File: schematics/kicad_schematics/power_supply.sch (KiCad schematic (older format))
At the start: 28 parts

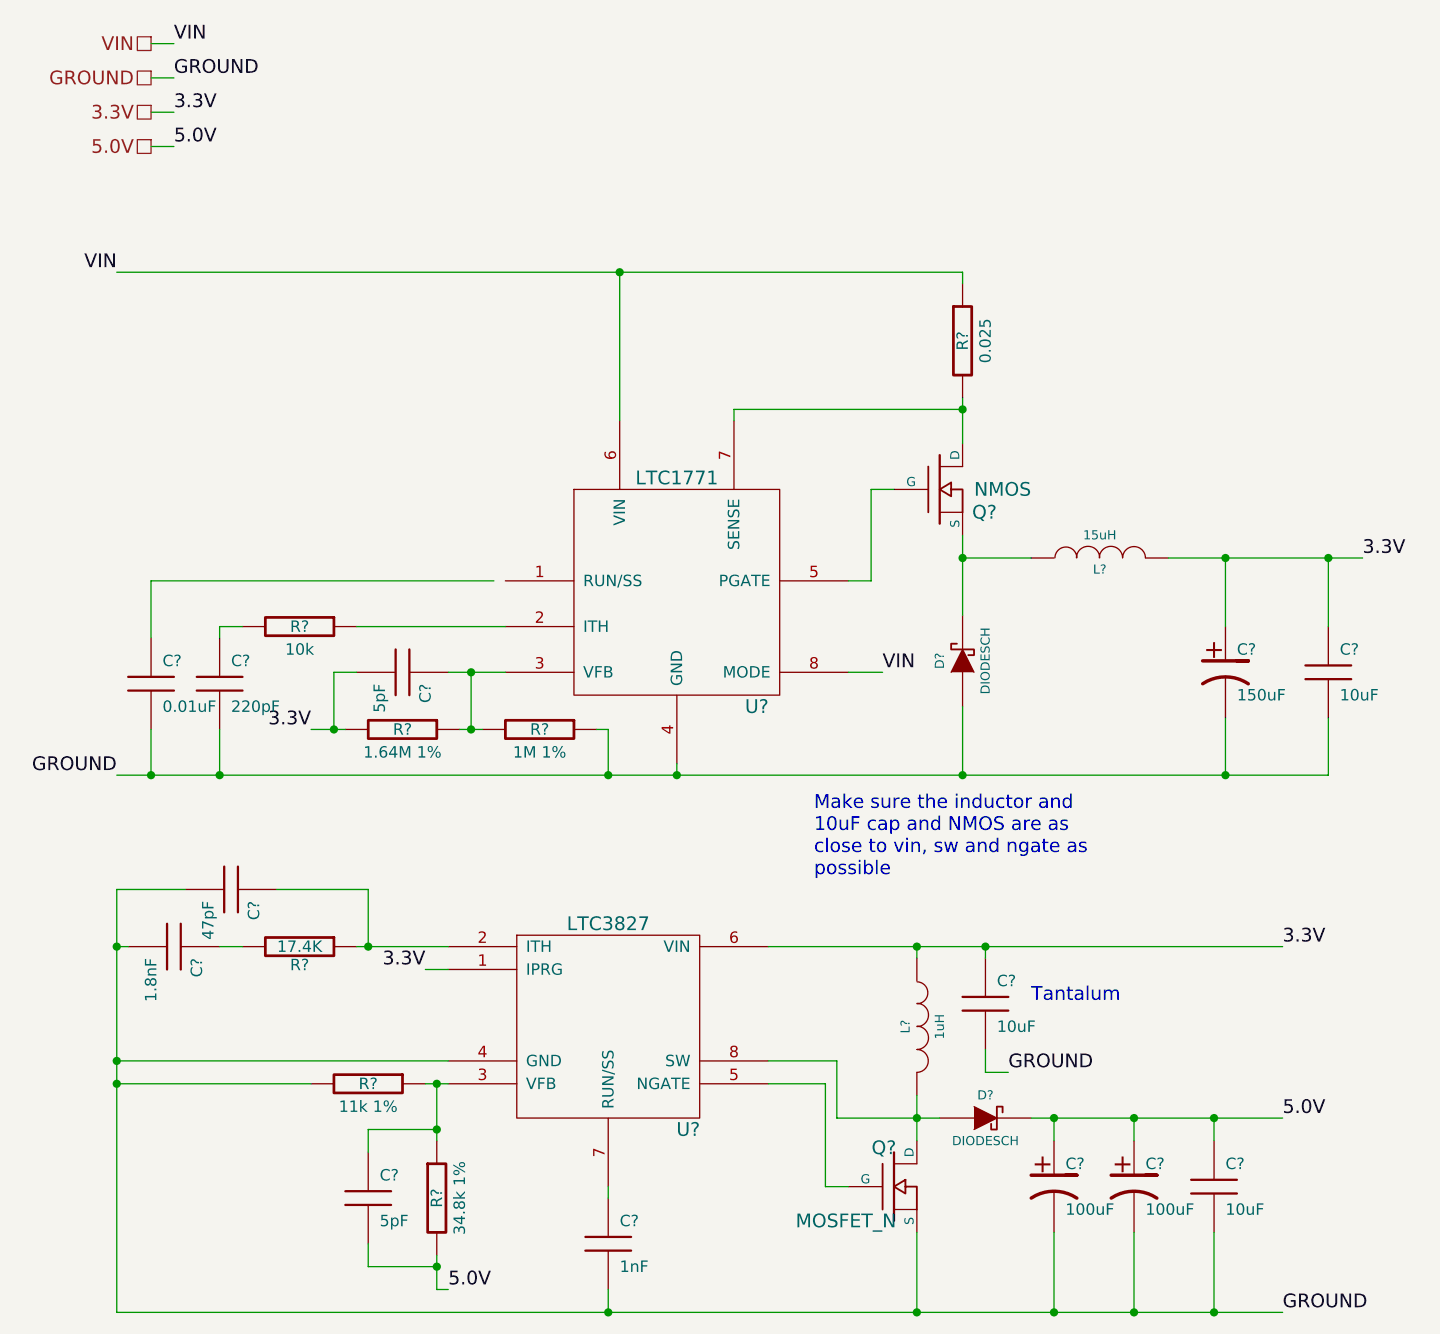
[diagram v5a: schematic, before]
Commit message: Cleaned up Schematic File and modified SD card module, bearboard schematic
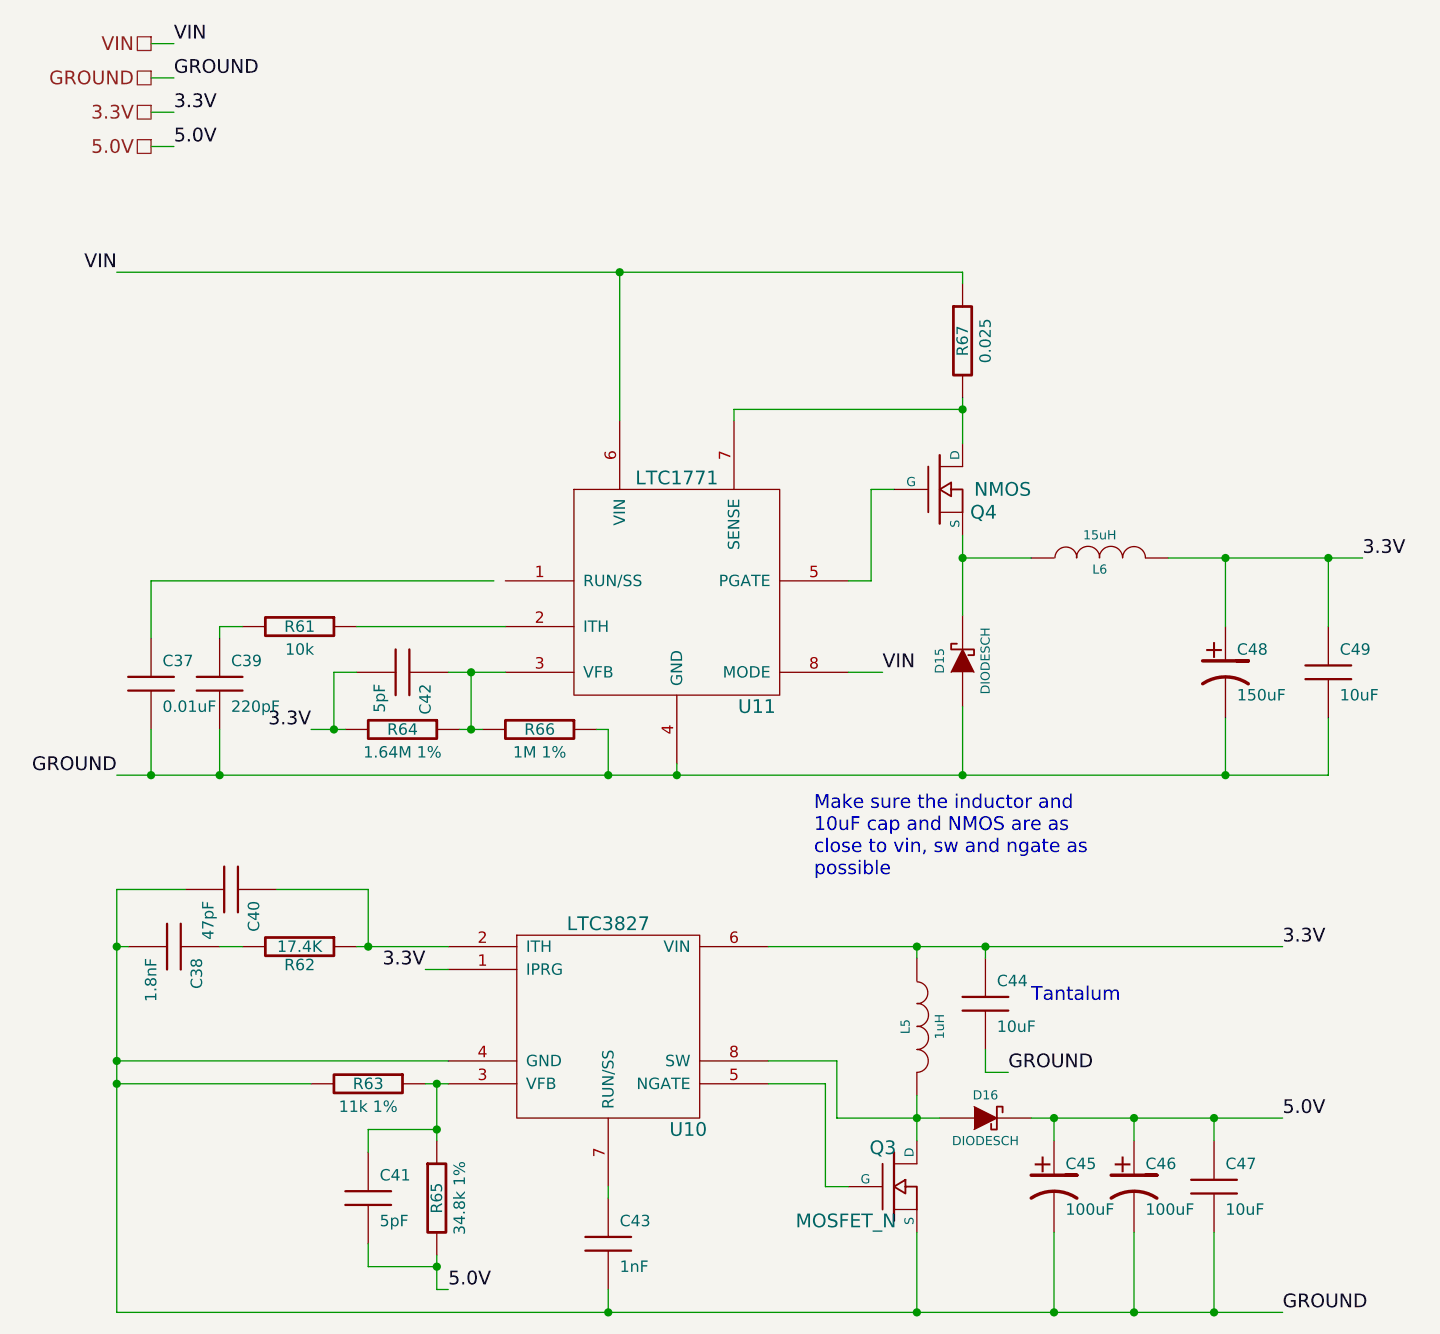
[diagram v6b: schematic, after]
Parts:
- gave numbers to parts that had none: 28
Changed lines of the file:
@@
-EESchema Schematic File Version 2  date Wed 10 Mar 2010 02:43:05 PM EST
+EESchema Schematic File Version 2  date Wed 10 Mar 2010 05:32:05 PM EST
 LIBS:power
 LIBS:device
@@
 5.0V
 $Comp
-L C C?
+L C C40
 U 1 1 4B8A7688
 P 2650 4450
-F 0 "C?" H 2700 4550 50  0000 L CNN
+F 0 "C40" H 2700 4550 50  0000 L CNN
 F 1 "47pF" H 2700 4350 50  0000 L CNN
 	1    2650 4450
@@
 $EndComp
 $Comp
-L C C?
+L C C38
 U 1 1 4B8A767D
 P 2400 4700
-F 0 "C?" H 2450 4800 50  0000 L CNN
+F 0 "C38" H 2450 4800 50  0000 L CNN
 F 1 "1.8nF" H 2450 4600 50  0000 L CNN
 	1    2400 4700
@@
 $EndComp
 $Comp
-L R R?
+L R R62
 U 1 1 4B8A766F
 P 2950 4700
-F 0 "R?" V 3030 4700 50  0000 C CNN
+F 0 "R62" V 3030 4700 50  0000 C CNN
 F 1 "17.4K" V 2950 4700 50  0000 C CNN
 	1    2950 4700
@@
 $EndComp
 $Comp
-L C C?
+L C C41
 U 1 1 4B8A761F
 P 3250 5800
-F 0 "C?" H 3300 5900 50  0000 L CNN
+F 0 "C41" H 3300 5900 50  0000 L CNN
 F 1 "5pF" H 3300 5700 50  0000 L CNN
 	1    3250 5800
@@
 5.0V
 $Comp
-L R R?
+L R R63
 U 1 1 4B8A758D
 P 3250 5300
-F 0 "R?" V 3250 5300 50  0000 C CNN
+F 0 "R63" V 3250 5300 50  0000 C CNN
 F 1 "11k 1%" V 3350 5300 50  0000 C CNN
 	1    3250 5300
@@
 $EndComp
 $Comp
-L R R?
+L R R65
 U 1 1 4B8A7583
 P 3550 5800
-F 0 "R?" V 3550 5800 50  0000 C CNN
+F 0 "R65" V 3550 5800 50  0000 C CNN
 F 1 "34.8k 1%" V 3650 5800 50  0000 C CNN
 	1    3550 5800
@@
 $EndComp
 $Comp
-L C C?
+L C C43
 U 1 1 4B8A753A
 P 4300 6000
-F 0 "C?" H 4350 6100 50  0000 L CNN
+F 0 "C43" H 4350 6100 50  0000 L CNN
 F 1 "1nF" H 4350 5900 50  0000 L CNN
 	1    4300 6000
@@
 GROUND
 $Comp
-L C C?
+L C C44
 U 1 1 4B8A7462
 P 5950 4950
-F 0 "C?" H 6000 5050 50  0000 L CNN
+F 0 "C44" H 6000 5050 50  0000 L CNN
 F 1 "10uF" H 6000 4850 50  0000 L CNN
 	1    5950 4950
@@
 GROUND
 $Comp
-L C C?
+L C C47
 U 1 1 4B8A73D4
 P 6950 5750
-F 0 "C?" H 7000 5850 50  0000 L CNN
+F 0 "C47" H 7000 5850 50  0000 L CNN
 F 1 "10uF" H 7000 5650 50  0000 L CNN
 	1    6950 5750
@@
 $EndComp
 $Comp
-L CP1 C?
+L CP1 C46
 U 1 1 4B8A73CB
 P 6600 5750
-F 0 "C?" H 6650 5850 50  0000 L CNN
+F 0 "C46" H 6650 5850 50  0000 L CNN
 F 1 "100uF" H 6650 5650 50  0000 L CNN
 	1    6600 5750
@@
 $EndComp
 $Comp
-L CP1 C?
+L CP1 C45
 U 1 1 4B8A73BE
 P 6250 5750
-F 0 "C?" H 6300 5850 50  0000 L CNN
+F 0 "C45" H 6300 5850 50  0000 L CNN
 F 1 "100uF" H 6300 5650 50  0000 L CNN
 	1    6250 5750
@@
 $EndComp
 $Comp
-L DIODESCH D?
+L DIODESCH D16
 U 1 1 4B8A73A8
 P 5950 5450
-F 0 "D?" H 5950 5550 40  0000 C CNN
+F 0 "D16" H 5950 5550 40  0000 C CNN
 F 1 "DIODESCH" H 5950 5350 40  0000 C CNN
 	1    5950 5450
@@
 $EndComp
 $Comp
-L INDUCTOR L?
+L INDUCTOR L5
 U 1 1 4B8A7363
 P 5650 5050
-F 0 "L?" V 5600 5050 40  0000 C CNN
+F 0 "L5" V 5600 5050 40  0000 C CNN
 F 1 "1uH" V 5750 5050 40  0000 C CNN
 	1    5650 5050
@@
 $EndComp
 $Comp
-L MOSFET_N Q?
+L MOSFET_N Q3
 U 1 1 4B8A7345
 P 5550 5750
-F 0 "Q?" H 5560 5920 60  0000 R CNN
+F 0 "Q3" H 5560 5920 60  0000 R CNN
 F 1 "MOSFET_N" H 5560 5600 60  0000 R CNN
 	1    5550 5750
@@
 $EndComp
 $Comp
-L LTC3827 U?
+L LTC3827 U10
 U 1 1 4B8A7318
 P 4300 5050
-F 0 "U?" H 4650 4600 60  0000 C CNN
+F 0 "U10" H 4650 4600 60  0000 C CNN
 F 1 "LTC3827" H 4300 5500 60  0000 C CNN
 	1    4300 5050
@@
 3.3V
 $Comp
-L C C?
+L C C42
 U 1 1 4B893539
 P 3400 3500
-F 0 "C?" H 3450 3600 50  0000 L CNN
+F 0 "C42" H 3450 3600 50  0000 L CNN
 F 1 "5pF" H 3450 3400 50  0000 L CNN
 	1    3400 3500
@@
 $EndComp
 $Comp
-L R R?
+L R R66
 U 1 1 4B893528
 P 4000 3750
-F 0 "R?" V 4000 3750 50  0000 C CNN
+F 0 "R66" V 4000 3750 50  0000 C CNN
 F 1 "1M 1%" V 4100 3750 50  0000 C CNN
 	1    4000 3750
@@
 $EndComp
 $Comp
-L R R?
+L R R64
 U 1 1 4B893518
 P 3400 3750
-F 0 "R?" V 3400 3750 50  0000 C CNN
+F 0 "R64" V 3400 3750 50  0000 C CNN
 F 1 "1.64M 1%" V 3500 3750 50  0000 C CNN
 	1    3400 3750
@@
 $EndComp
 $Comp
-L C C?
+L C C39
 U 1 1 4B8934DD
 P 2600 3550
-F 0 "C?" H 2650 3650 50  0000 L CNN
+F 0 "C39" H 2650 3650 50  0000 L CNN
 F 1 "220pF" H 2650 3450 50  0000 L CNN
 	1    2600 3550
@@
 $EndComp
 $Comp
-L R R?
+L R R61
 U 1 1 4B8934CE
 P 2950 3300
-F 0 "R?" V 2950 3300 50  0000 C CNN
+F 0 "R61" V 2950 3300 50  0000 C CNN
 F 1 "10k" V 3050 3300 50  0000 C CNN
 	1    2950 3300
@@
 $EndComp
 $Comp
-L C C?
+L C C37
 U 1 1 4B8934B4
 P 2300 3550
-F 0 "C?" H 2350 3650 50  0000 L CNN
+F 0 "C37" H 2350 3650 50  0000 L CNN
 F 1 "0.01uF" H 2350 3450 50  0000 L CNN
 	1    2300 3550
@@
 $EndComp
 $Comp
-L C C?
+L C C49
 U 1 1 4B893480
 P 7450 3500
-F 0 "C?" H 7500 3600 50  0000 L CNN
+F 0 "C49" H 7500 3600 50  0000 L CNN
 F 1 "10uF" H 7500 3400 50  0000 L CNN
 	1    7450 3500
@@
 VIN
 $Comp
-L CP1 C?
+L CP1 C48
 U 1 1 4B89335E
 P 7000 3500
-F 0 "C?" H 7050 3600 50  0000 L CNN
+F 0 "C48" H 7050 3600 50  0000 L CNN
 F 1 "150uF" H 7050 3400 50  0000 L CNN
 	1    7000 3500
@@
 $EndComp
 $Comp
-L INDUCTOR L?
+L INDUCTOR L6
 U 1 1 4B8932D4
 P 6450 3000
-F 0 "L?" V 6400 3000 40  0000 C CNN
+F 0 "L6" V 6400 3000 40  0000 C CNN
 F 1 "15uH" V 6550 3000 40  0000 C CNN
 	1    6450 3000
@@
 VIN
 $Comp
-L DIODESCH D?
+L DIODESCH D15
 U 1 1 4B8931FF
 P 5850 3450
-F 0 "D?" H 5850 3550 40  0000 C CNN
+F 0 "D15" H 5850 3550 40  0000 C CNN
 F 1 "DIODESCH" H 5850 3350 40  0000 C CNN
 	1    5850 3450
@@
 $EndComp
 $Comp
-L R R?
+L R R67
 U 1 1 4B893191
 P 5850 2050
-F 0 "R?" V 5850 2050 50  0000 C CNN
+F 0 "R67" V 5850 2050 50  0000 C CNN
 F 1 "0.025" V 5950 2050 50  0000 C CNN
 	1    5850 2050
@@
 $EndComp
 $Comp
-L MOSFET_N Q?
+L MOSFET_N Q4
 U 1 1 4B893175
 P 5750 2700
-F 0 "Q?" H 6000 2600 60  0000 R CNN
+F 0 "Q4" H 6000 2600 60  0000 R CNN
 F 1 "NMOS" H 6150 2700 60  0000 R CNN
 	1    5750 2700
@@
 $EndComp
 $Comp
-L LTC1771 U?
+L LTC1771 U11
 U 1 1 4B893166
 P 4600 3150
-F 0 "U?" H 4950 2650 60  0000 C CNN
+F 0 "U11" H 4950 2650 60  0000 C CNN
 F 1 "LTC1771" H 4600 3650 60  0000 C CNN
 	1    4600 3150

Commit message: Updated USB connector to change the sheild pin to power input Updated the schematic to fix some schematic electrical issues
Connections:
- net at U11.1 (RUN/SS): now also C37.1
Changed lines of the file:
@@
-EESchema Schematic File Version 2  date Wed 10 Mar 2010 05:32:05 PM EST
+EESchema Schematic File Version 2  date Wed 10 Mar 2010 08:20:30 PM EST
 LIBS:power
 LIBS:device
@@
 EELAYER END
 $Descr A4 11700 8267
-Sheet 2 5
+Sheet 3 5
 Title ""
-Date "10 mar 2010"
+Date "11 mar 2010"
 Rev ""
 Comp ""
@@
 Comment4 ""
 $EndDescr
+Wire Wire Line
+	3850 3100 2300 3100
+Connection ~ 2150 4700
+Connection ~ 2150 5200
+Wire Wire Line
+	2150 4450 2150 6300
+Wire Wire Line
+	2150 4450 2450 4450
+Wire Wire Line
+	2150 4700 2200 4700
+Wire Wire Line
+	3200 4700 3600 4700
+Connection ~ 3550 5500
+Wire Wire Line
+	3550 5500 3250 5500
+Wire Wire Line
+	3250 5500 3250 5600
+Wire Wire Line
+	3000 5300 2150 5300
+Wire Wire Line
+	2150 5200 3600 5200
+Wire Wire Line
+	3600 5300 3500 5300
+Wire Wire Line
+	3600 6200 3550 6200
+Wire Wire Line
+	3550 6200 3550 6050
+Connection ~ 5650 6300
+Wire Wire Line
+	4300 6200 4300 6300
+Connection ~ 5950 4700
+Wire Wire Line
+	5950 4700 5950 4750
+Connection ~ 5650 4700
+Wire Wire Line
+	5000 4700 7250 4700
+Wire Wire Line
+	6950 6300 6950 5950
+Connection ~ 6250 6300
+Wire Wire Line
+	6250 6300 6250 5950
+Connection ~ 6250 5450
+Wire Wire Line
+	6250 5450 6250 5550
+Wire Wire Line
+	6950 5550 6950 5450
+Wire Wire Line
+	5350 5750 5250 5750
+Wire Wire Line
+	5250 5750 5250 5300
+Wire Wire Line
+	5250 5300 5000 5300
+Wire Wire Line
+	5650 5550 5650 5350
+Wire Wire Line
+	2300 1050 2400 1050
+Wire Wire Line
+	2300 750  2400 750
+Wire Wire Line
+	3100 3750 3100 3500
+Wire Wire Line
+	3100 3500 3200 3500
+Connection ~ 3700 3750
+Wire Wire Line
+	3700 3750 3700 3500
+Connection ~ 4300 3950
+Wire Wire Line
+	4300 3950 4300 3750
+Wire Wire Line
+	4300 3750 4250 3750
+Wire Wire Line
+	3200 3300 3850 3300
+Connection ~ 2300 3950
+Wire Wire Line
+	2300 3750 2300 3950
+Connection ~ 7000 3950
+Wire Wire Line
+	2150 3950 7450 3950
+Wire Wire Line
+	7450 3950 7450 3700
+Wire Wire Line
+	7600 3000 6750 3000
+Wire Wire Line
+	5500 3500 5350 3500
+Wire Wire Line
+	7000 3000 7000 3300
+Connection ~ 4600 3950
+Wire Wire Line
+	2150 1750 5850 1750
+Wire Wire Line
+	5350 3100 5450 3100
+Wire Wire Line
+	5450 3100 5450 2700
+Wire Wire Line
+	5450 2700 5550 2700
+Wire Wire Line
+	4350 2400 4350 1750
+Wire Wire Line
+	5850 1750 5850 1800
+Wire Wire Line
+	5850 2500 5850 2300
+Wire Wire Line
+	5850 2350 4850 2350
+Wire Wire Line
+	4850 2350 4850 2400
+Connection ~ 5850 2350
+Wire Wire Line
+	5850 3250 5850 2900
+Connection ~ 4350 1750
+Wire Wire Line
+	5850 3950 5850 3650
+Wire Wire Line
+	4600 3950 4600 3900
+Wire Wire Line
+	6150 3000 5850 3000
+Connection ~ 5850 3000
+Wire Wire Line
+	7000 3700 7000 3950
+Connection ~ 5850 3950
+Connection ~ 7000 3000
+Wire Wire Line
+	7450 3300 7450 3000
+Connection ~ 7450 3000
+Wire Wire Line
+	2600 3350 2600 3300
+Wire Wire Line
+	2600 3300 2700 3300
+Wire Wire Line
+	2600 3950 2600 3750
+Connection ~ 2600 3950
+Wire Wire Line
+	3750 3750 3650 3750
+Wire Wire Line
+	3850 3500 3600 3500
+Connection ~ 3700 3500
+Wire Wire Line
+	3000 3750 3150 3750
+Connection ~ 3100 3750
+Wire Wire Line
+	2300 900  2400 900
+Wire Wire Line
+	5650 4750 5650 4700
+Wire Wire Line
+	5000 5200 5300 5200
+Wire Wire Line
+	5300 5200 5300 5450
+Connection ~ 5650 5450
+Wire Wire Line
+	5300 5450 5750 5450
+Wire Wire Line
+	6600 5450 6600 5550
+Connection ~ 6600 5450
+Wire Wire Line
+	5650 6300 5650 5950
+Wire Wire Line
+	6600 6300 6600 5950
+Connection ~ 6600 6300
+Connection ~ 6950 6300
+Wire Wire Line
+	5950 5150 5950 5250
+Wire Wire Line
+	5950 5250 6050 5250
+Wire Wire Line
+	7250 5450 6150 5450
+Connection ~ 6950 5450
+Wire Wire Line
+	4300 5800 4300 5750
+Wire Wire Line
+	3600 4800 3500 4800
+Wire Wire Line
+	3550 5550 3550 5300
+Connection ~ 3550 5300
+Wire Wire Line
+	2150 6300 7250 6300
+Connection ~ 4300 6300
+Connection ~ 2150 5300
+Wire Wire Line
+	3250 6000 3250 6100
+Wire Wire Line
+	3250 6100 3550 6100
+Connection ~ 3550 6100
+Wire Wire Line
+	2700 4700 2600 4700
+Wire Wire Line
+	2850 4450 3250 4450
+Wire Wire Line
+	3250 4450 3250 4700
+Connection ~ 3250 4700
+Wire Wire Line
+	2300 1200 2400 1200
+Wire Wire Line
+	2300 3100 2300 3350
 Text Label 2400 1200 0    60   ~ 0
 5.0V
-Wire Wire Line
-	2300 1200 2400 1200
-Connection ~ 3250 4700
-Wire Wire Line
-	3250 4700 3250 4450
-Wire Wire Line
-	3250 4450 2850 4450
-Wire Wire Line
-	2700 4700 2600 4700
-Connection ~ 3550 6100
-Wire Wire Line
-	3550 6100 3250 6100
-Wire Wire Line
-	3250 6100 3250 6000
-Connection ~ 2150 5300
-Connection ~ 4300 6300
-Wire Wire Line
-	7250 6300 2150 6300
-Connection ~ 3550 5300
-Wire Wire Line
-	3550 5550 3550 5300
-Wire Wire Line
-	3600 4800 3500 4800
-Wire Wire Line
-	4300 5800 4300 5750
-Connection ~ 6950 5450
-Wire Wire Line
-	7250 5450 6150 5450
-Wire Wire Line
-	6050 5250 5950 5250
-Wire Wire Line
-	5950 5250 5950 5150
-Connection ~ 6950 6300
-Connection ~ 6600 6300
-Wire Wire Line
-	6600 6300 6600 5950
-Wire Wire Line
-	5650 6300 5650 5950
-Connection ~ 6600 5450
-Wire Wire Line
-	6600 5450 6600 5550
-Wire Wire Line
-	5750 5450 5300 5450
-Connection ~ 5650 5450
-Wire Wire Line
-	5300 5450 5300 5200
-Wire Wire Line
-	5300 5200 5000 5200
-Wire Wire Line
-	5650 4750 5650 4700
-Wire Wire Line
-	2300 900  2400 900
-Connection ~ 3100 3750
-Wire Wire Line
-	3000 3750 3150 3750
-Connection ~ 3700 3500
-Wire Wire Line
-	3850 3500 3600 3500
-Wire Wire Line
-	3750 3750 3650 3750
-Connection ~ 2600 3950
-Wire Wire Line
-	2600 3950 2600 3750
-Wire Wire Line
-	2700 3300 2600 3300
-Wire Wire Line
-	2600 3300 2600 3350
-Wire Wire Line
-	2300 3350 2300 3100
-Wire Wire Line
-	2300 3100 3800 3100
-Connection ~ 7450 3000
-Wire Wire Line
-	7450 3300 7450 3000
-Connection ~ 7000 3000
-Connection ~ 5850 3950
-Wire Wire Line
-	7000 3700 7000 3950
-Connection ~ 5850 3000
-Wire Wire Line
-	6150 3000 5850 3000
-Wire Wire Line
-	4600 3950 4600 3900
-Wire Wire Line
-	5850 3950 5850 3650
-Connection ~ 4350 1750
-Wire Wire Line
-	5850 3250 5850 2900
-Connection ~ 5850 2350
-Wire Wire Line
-	4850 2400 4850 2350
-Wire Wire Line
-	4850 2350 5850 2350
-Wire Wire Line
-	5850 2500 5850 2300
-Wire Wire Line
-	5850 1800 5850 1750
-Wire Wire Line
-	4350 2400 4350 1750
-Wire Wire Line
-	5550 2700 5450 2700
-Wire Wire Line
-	5450 2700 5450 3100
-Wire Wire Line
-	5450 3100 5350 3100
-Wire Wire Line
-	5850 1750 2150 1750
-Connection ~ 4600 3950
-Wire Wire Line
-	7000 3000 7000 3300
-Wire Wire Line
-	5500 3500 5350 3500
-Wire Wire Line
-	7600 3000 6750 3000
-Wire Wire Line
-	7450 3700 7450 3950
-Wire Wire Line
-	7450 3950 2150 3950
-Connection ~ 7000 3950
-Wire Wire Line
-	2300 3750 2300 3950
-Connection ~ 2300 3950
-Wire Wire Line
-	3200 3300 3850 3300
-Wire Wire Line
-	4250 3750 4300 3750
-Wire Wire Line
-	4300 3750 4300 3950
-Connection ~ 4300 3950
-Wire Wire Line
-	3700 3750 3700 3500
-Connection ~ 3700 3750
-Wire Wire Line
-	3200 3500 3100 3500
-Wire Wire Line
-	3100 3500 3100 3750
-Wire Wire Line
-	2300 750  2400 750
-Wire Wire Line
-	2300 1050 2400 1050
-Wire Wire Line
-	5650 5550 5650 5350
-Wire Wire Line
-	5000 5300 5250 5300
-Wire Wire Line
-	5250 5300 5250 5750
-Wire Wire Line
-	5250 5750 5350 5750
-Wire Wire Line
-	6950 5550 6950 5450
-Wire Wire Line
-	6250 5450 6250 5550
-Connection ~ 6250 5450
-Wire Wire Line
-	6250 6300 6250 5950
-Connection ~ 6250 6300
-Wire Wire Line
-	6950 6300 6950 5950
-Wire Wire Line
-	5000 4700 7250 4700
-Connection ~ 5650 4700
-Wire Wire Line
-	5950 4700 5950 4750
-Connection ~ 5950 4700
-Wire Wire Line
-	4300 6200 4300 6300
-Connection ~ 5650 6300
-Wire Wire Line
-	3550 6050 3550 6200
-Wire Wire Line
-	3550 6200 3600 6200
-Wire Wire Line
-	3600 5300 3500 5300
-Wire Wire Line
-	2150 5200 3600 5200
-Wire Wire Line
-	3000 5300 2150 5300
-Wire Wire Line
-	3250 5600 3250 5500
-Wire Wire Line
-	3250 5500 3550 5500
-Connection ~ 3550 5500
-Wire Wire Line
-	3200 4700 3600 4700
-Wire Wire Line
-	2150 4700 2200 4700
-Wire Wire Line
-	2450 4450 2150 4450
-Wire Wire Line
-	2150 4450 2150 6300
-Connection ~ 2150 5200
-Connection ~ 2150 4700
 Text HLabel 2300 1200 0    60   UnSpc ~ 0
 5.0V
